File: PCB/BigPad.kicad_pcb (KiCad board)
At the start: 2 copper layers, 111.9 x 64.3 mm, 25 parts

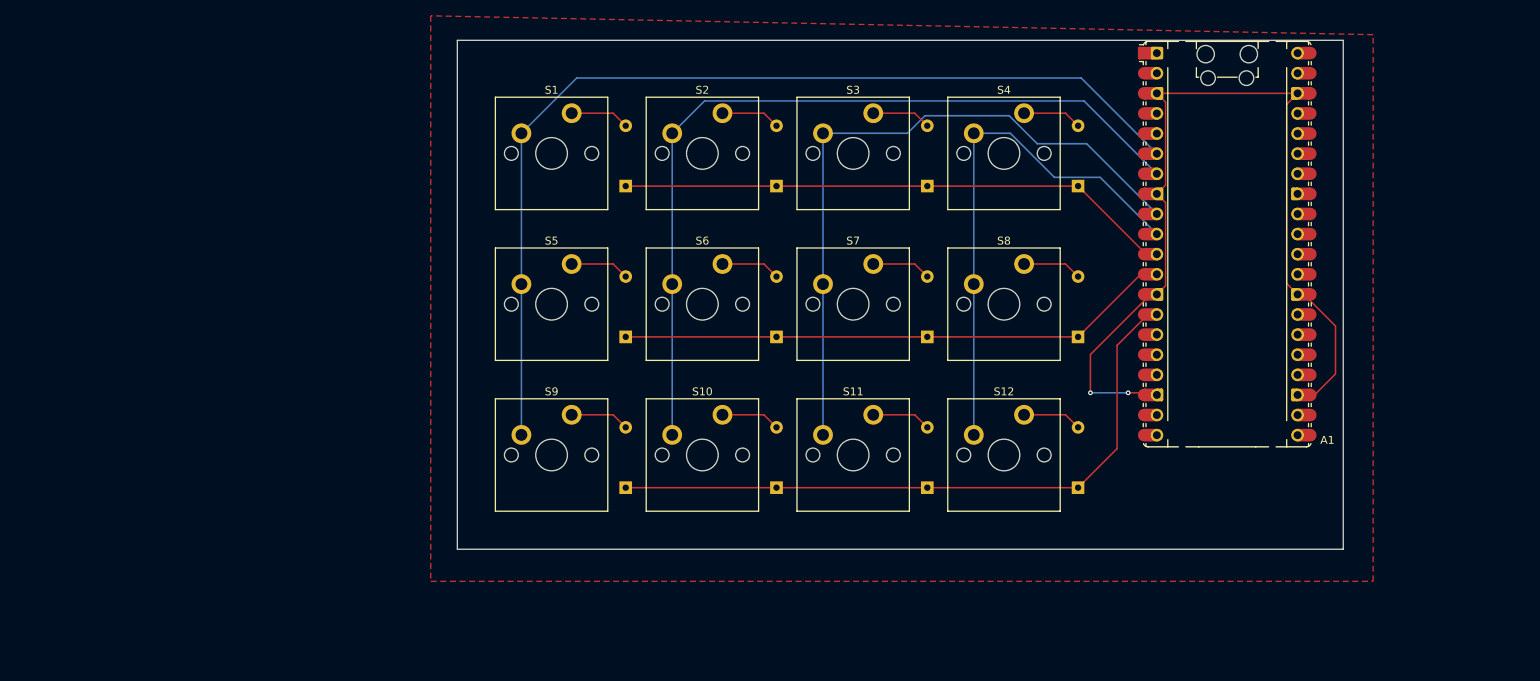
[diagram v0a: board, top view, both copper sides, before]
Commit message: completed rotary encoders in PCB design
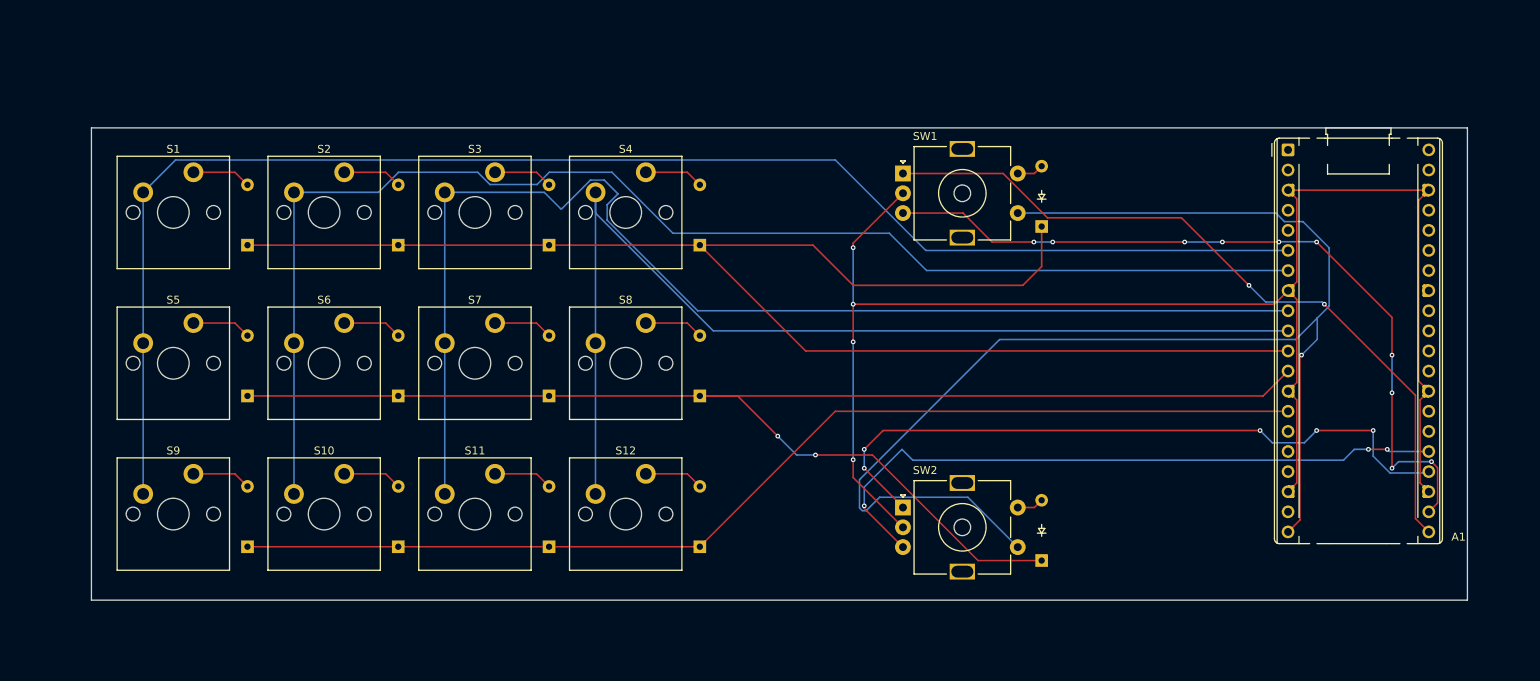
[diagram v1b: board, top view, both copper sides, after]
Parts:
- added D13: ~, ScottoKeebs_Components:Diode_DO-35, F.Cu at (172.4, 83.8)
- added D14: ~, ScottoKeebs_Components:Diode_DO-35, F.Cu at (172.4, 126.0)
- added SW1: RotaryEncoder_Switch, Rotary_Encoder:RotaryEncoder_Alps_EC11E-Switch_Vertical_H20mm_MountingHoles, F.Cu at (154.9, 77.1)
- added SW2: RotaryEncoder_Switch, Rotary_Encoder:RotaryEncoder_Alps_EC11E-Switch_Vertical_H20mm_MountingHoles, F.Cu at (154.9, 119.3)
- A1: footprint Module:RaspberryPi_Pico_Common_Unspecified -> Module:RaspberryPi_Pico_Common_THT
- moved D1 48.4 mm to (72.1, 86.1)
- moved D11 48.4 mm to (110.2, 124.2)
- moved D3 48.4 mm to (110.2, 86.1)
- moved D5 48.4 mm to (72.1, 105.2)
- moved D7 48.4 mm to (110.2, 105.2)
- moved D9 48.4 mm to (72.1, 124.2)
- moved S11 48.4 mm to (100.8, 120.1)
- moved S3 48.4 mm to (100.8, 82.0)
- moved S7 48.4 mm to (100.8, 101.0)
- moved D10 48.4 mm to (91.2, 124.2)
- moved D12 48.4 mm to (129.3, 124.2)
- moved D2 48.4 mm to (91.2, 86.1)
- moved D4 48.4 mm to (129.3, 86.1)
- moved D6 48.4 mm to (91.2, 105.2)
- moved D8 48.4 mm to (129.3, 105.2)
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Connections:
- A1 pad 20: unconnected-(A1-GPIO15-Pad20) -> /Column 4
- A1 pad 21: unconnected-(A1-GPIO16-Pad21) -> Net-(A1-GPIO16)
- A1 pad 22: unconnected-(A1-GPIO17-Pad22) -> Net-(A1-GPIO17)
- A1 pad 24: unconnected-(A1-GPIO18-Pad24) -> Net-(A1-GPIO18)
- A1 pad 25: unconnected-(A1-GPIO19-Pad25) -> Net-(A1-GPIO19)
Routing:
- net /Column 4: track 0.00 -> 172.5 mm, vias 0 -> 1
- net /Row 0: track 70.7 -> 188.3 mm
- net /Row 1: track 70.4 -> 184.6 mm, vias 0 -> 2
- net Net-(A1-GPIO17): track 0.00 -> 98.8 mm, vias 0 -> 10
- net Net-(A1-GPIO16): track 0.00 -> 94.3 mm, vias 0 -> 2
- net Net-(A1-GPIO18): track 0.00 -> 87.2 mm, vias 0 -> 5
- net Net-(A1-GND-Pad13): track 114.8 -> 201.8 mm, vias 2 -> 4
- net Net-(A1-GPIO19): track 0.00 -> 84.2 mm, vias 0 -> 3
- net /Column 2: track 86.3 -> 157.7 mm
- net /Column 3: track 66.5 -> 134.4 mm
- net /Column 1: track 104.8 -> 171.2 mm
- net /Column 0: track 125.2 -> 189.2 mm
- net /Row 2: track 83.8 -> 138.5 mm
- net Net-(D14-A): track 0.00 -> 3.40 mm
- net Net-(D13-A): track 0.00 -> 3.40 mm
- removed copper zone on F.Cu, net (none)
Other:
- board size 111.9 x 64.3 mm -> 173.8 x 59.7 mm

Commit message: added m3 screw holes to pcb
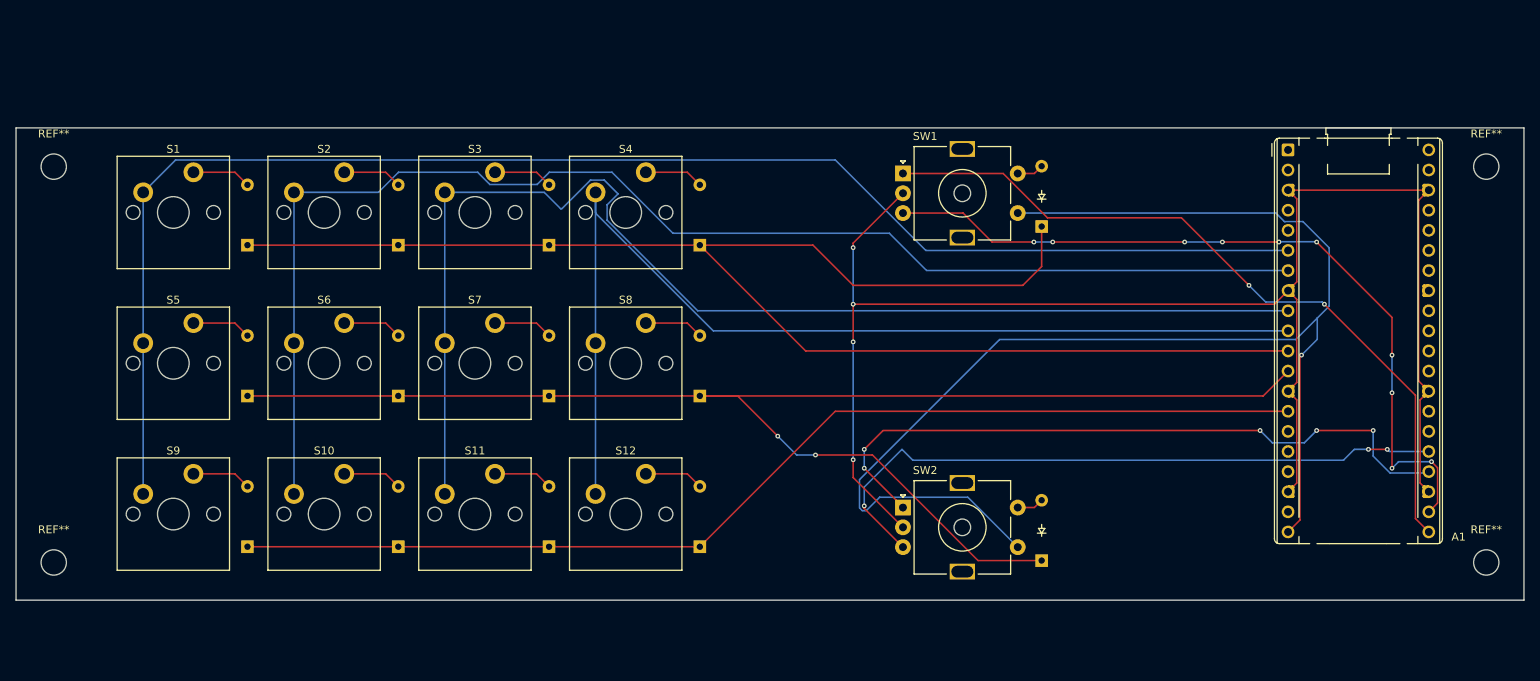
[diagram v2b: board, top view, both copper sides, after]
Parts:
- added REF**: MountingHole_3.2mm_M3, MountingHole:MountingHole_3.2mm_M3, F.Cu at (47.6, 76.2)
- added REF**: MountingHole_3.2mm_M3, MountingHole:MountingHole_3.2mm_M3, F.Cu at (47.6, 126.2)
- added REF**: MountingHole_3.2mm_M3, MountingHole:MountingHole_3.2mm_M3, F.Cu at (228.6, 76.2)
- added REF**: MountingHole_3.2mm_M3, MountingHole:MountingHole_3.2mm_M3, F.Cu at (228.6, 126.2)
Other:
- board size 173.8 x 59.7 mm -> 190.5 x 59.7 mm

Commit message: fixed several wiring issues
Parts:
- removed the REF** at (47.6, 76.2)
- removed the REF** at (47.6, 126.2)
- removed the REF** at (228.6, 76.2)
- removed the REF** at (228.6, 126.2)
- added REF**: MountingHole_3.2mm_M3, MountingHole:MountingHole_3.2mm_M3, F.Cu at (47.0, 81.1)
- added REF**: MountingHole_3.2mm_M3, MountingHole:MountingHole_3.2mm_M3, F.Cu at (47.0, 132.2)
- added REF**: MountingHole_3.2mm_M3, MountingHole:MountingHole_3.2mm_M3, F.Cu at (228.0, 81.1)
- added REF**: MountingHole_3.2mm_M3, MountingHole:MountingHole_3.2mm_M3, F.Cu at (228.0, 132.2)
- D1, D10, D11, D12, D2, D3, D4, D5, D6, D7, D8, D9: footprint ScottoKeebs_Components:Diode_DO-35 -> Diode_SMD:D_SOD-123; moved to F.Cu
- D13, D14: footprint ScottoKeebs_Components:Diode_DO-35 -> Diode_SMD:D_SOD-123
- S1, S10, S11, S12, S2, S3, S4, S5, S6, S7, S8, S9: footprint ScottoKeebs_MX:MX_PCB_1.00u -> PCM_Switch_Keyboard_Hotswap_Kailh:SW_Hotswap_Kailh_MX_Plated_1.00u
- moved S1 4.12 mm to (61.3, 85.8), turned to 180 degrees
- moved S2 4.12 mm to (80.3, 85.8), turned to 180 degrees
- moved S4 4.12 mm to (118.4, 85.8), turned to 180 degrees
- moved SW1 4.12 mm to (153.4, 80.9)
- moved SW2 4.12 mm to (153.4, 123.1)
- moved S3 4.12 mm to (99.4, 85.8), turned to 180 degrees
- moved S10 4.12 mm to (80.3, 123.9), turned to 180 degrees
- moved S12 4.12 mm to (118.4, 123.9), turned to 180 degrees
- moved S5 4.12 mm to (61.3, 104.9), turned to 180 degrees
- moved S6 4.12 mm to (80.3, 104.9), turned to 180 degrees
- moved S8 4.12 mm to (118.4, 104.9), turned to 180 degrees
- moved S9 4.12 mm to (61.3, 123.9), turned to 180 degrees
- moved S11 4.12 mm to (99.4, 123.9), turned to 180 degrees
- moved S7 4.12 mm to (99.4, 104.9), turned to 180 degrees
- moved A1 4.12 mm to (202.1, 77.9)
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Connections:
- net Net-(A1-GND-Pad13) renamed GND
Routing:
- net GND: track 201.8 -> 7.03 mm, vias 4 -> 0
- net /Column 4: track 172.5 -> 78.2 mm
- net /Row 0: track 188.3 -> 144.5 mm
- net /Row 1: track 184.6 -> 148.6 mm, vias 2 -> 0
- net Net-(A1-GPIO16): track 94.3 -> 116.5 mm, vias 2 -> 3
- net Net-(A1-GPIO18): track 87.2 -> 71.9 mm
- net /Column 2: track 157.7 -> 144.1 mm, vias 0 -> 2
- net /Column 3: track 134.4 -> 123.1 mm, vias 0 -> 2
- net Net-(A1-GPIO19): track 84.2 -> 74.1 mm, vias 3 -> 1
- net /Column 1: track 171.2 -> 162.0 mm, vias 0 -> 2
- net Net-(D9-A): track 7.48 -> 13.5 mm
- net Net-(D5-A): track 7.48 -> 13.5 mm
- net Net-(D10-A): track 7.48 -> 13.5 mm
- net Net-(D1-A): track 7.48 -> 13.5 mm
- net Net-(D12-A): track 7.48 -> 13.5 mm
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- added copper zone on B.Cu, net GND
- added copper zone on F.Cu, net GND
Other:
- board size 190.5 x 59.7 mm -> 188.5 x 65.5 mm
